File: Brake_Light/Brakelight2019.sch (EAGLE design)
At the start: 62 parts, among them J1 POWER_JACK, U1 R-78E5.0-1.0

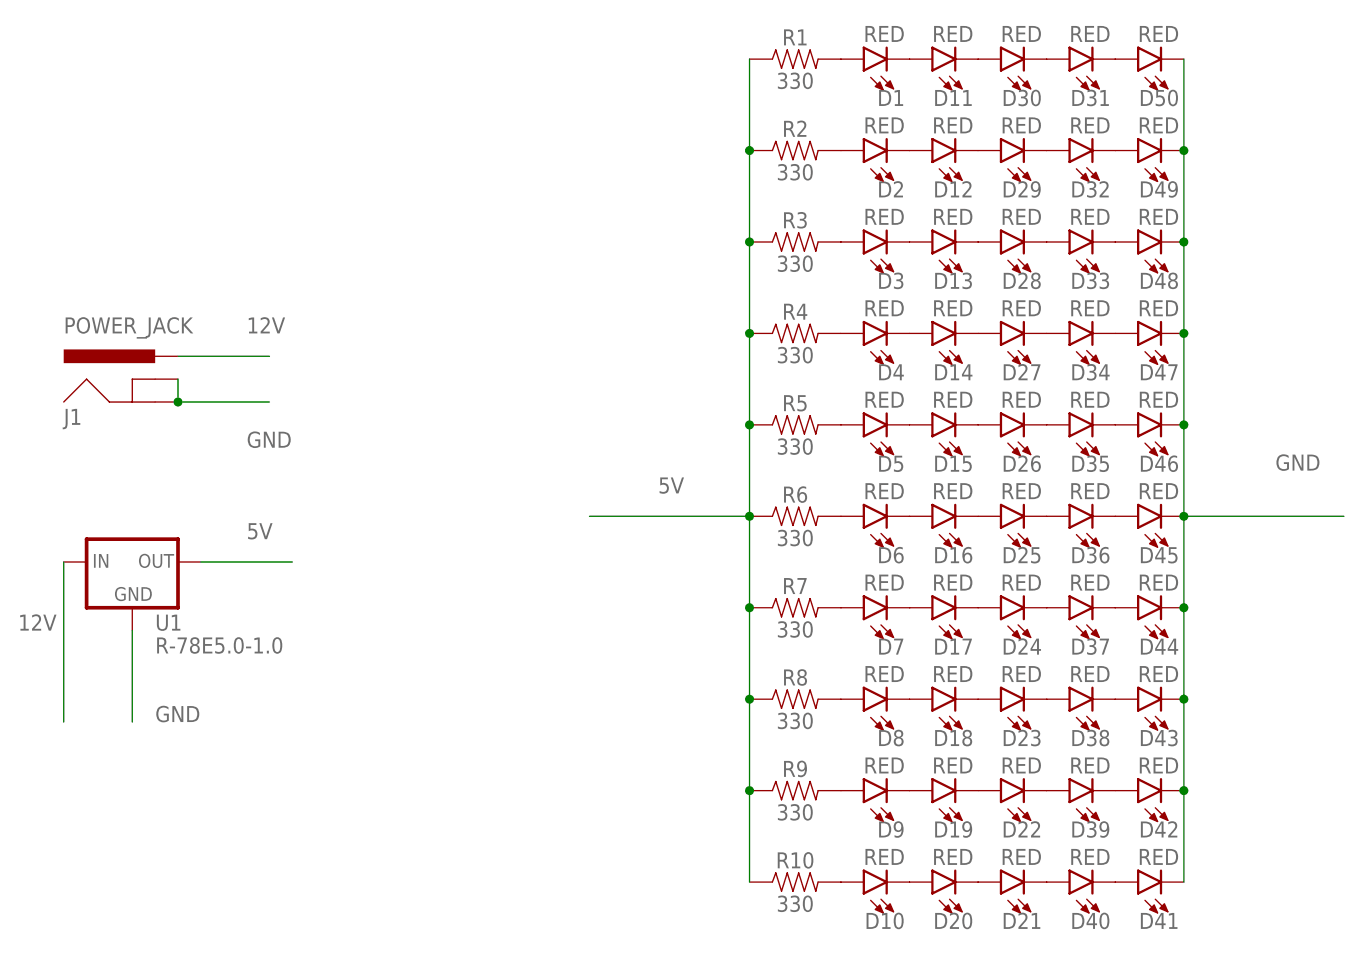
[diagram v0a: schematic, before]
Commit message: Add files via upload
changed out LEDs and voltage regulator for better ones.
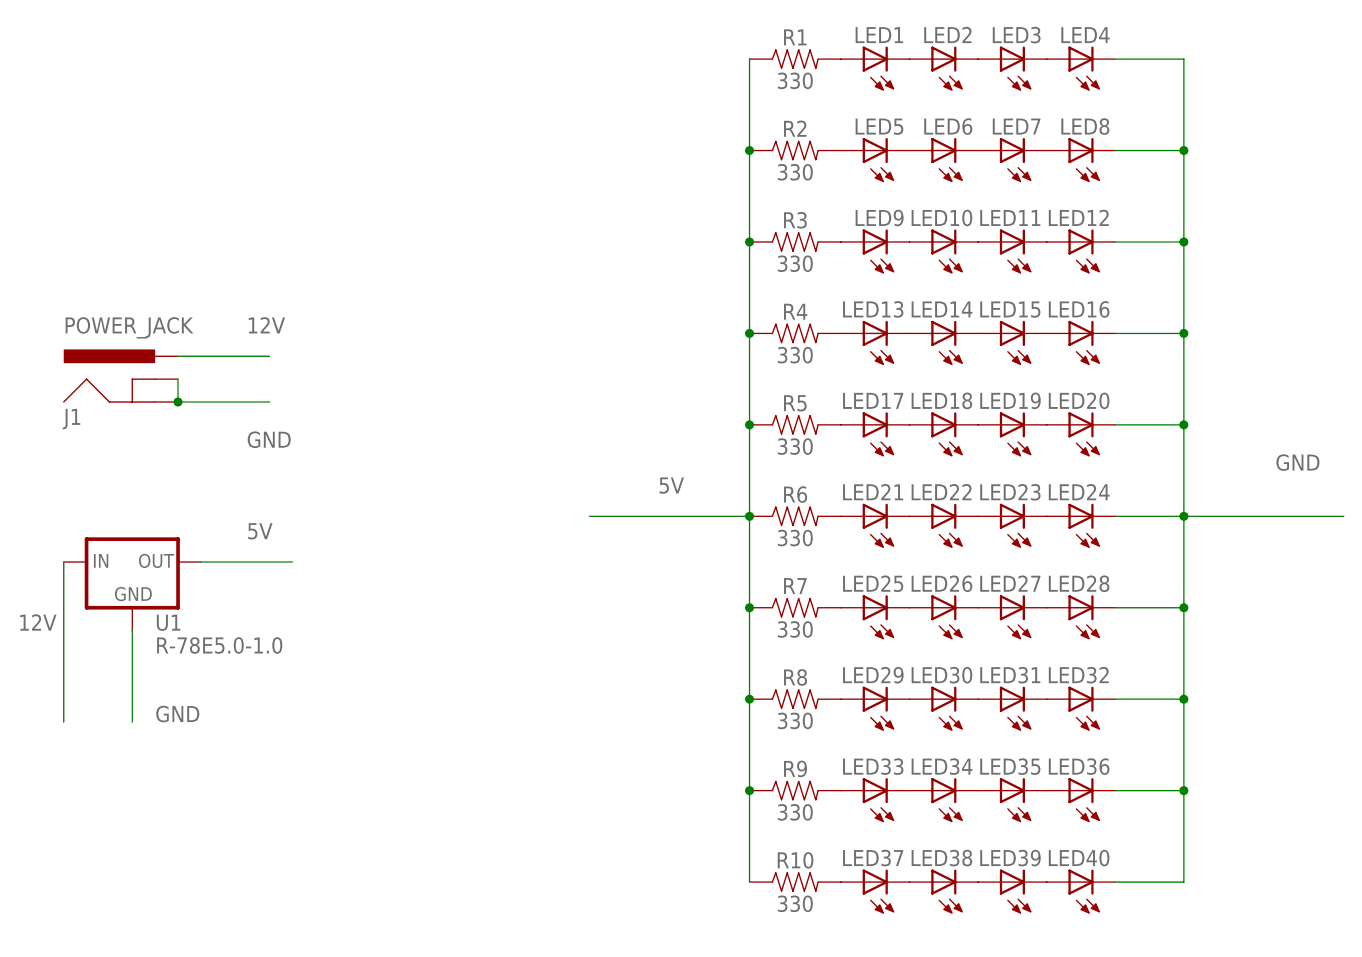
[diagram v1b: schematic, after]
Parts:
- removed D1, D10, D11, D12, D13, D14, D15, D16, D17, D18, D19, D2, D20, D21, D22, D23, D24, D25, D26, D27, D28, D29, D3, D30, D31, D32, D33, D34, D35, D36, D37, D38, D39, D4, D40, D41, D42, D43, D44, D45, D46, D47, D48, D49, D5, D50, D6, D7, D8, D9: RED, SparkFun-LED:LED-RED1206
- added LED1, LED10, LED11, LED12, LED13, LED14, LED15, LED16, LED17, LED18, LED19, LED2, LED20, LED21, LED22, LED23, LED24, LED25, LED26, LED27, LED28, LED29, LED3, LED30, LED31, LED32, LED33, LED34, LED35, LED36, LED37, LED38, LED39, LED4, LED40, LED5, LED6, LED7, LED8, LED9: (no value), adafruit:LED5MM
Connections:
- removed net N$41: D1.A, R1.2
- removed net N$42: D2.A, R2.2
- removed net N$43: D3.A, R3.2
- removed net N$44: D4.A, R4.2
- removed net N$45: D5.A, R5.2
- removed net N$46: D6.A, R6.2
- removed net N$47: D7.A, R7.2
- removed net N$48: D8.A, R8.2
- removed net N$49: D9.A, R9.2
- removed net N$50: D10.A, R10.2
- net GND: now also LED12.C, LED16.C, LED20.C, LED24.C, LED28.C, LED32.C, LED36.C, LED4.C, LED40.C, LED8.C; no longer D41.C, D42.C, D43.C, D44.C, D45.C, D46.C, D47.C, D48.C, D49.C, D50.C
- net N$1: now also LED1.A, R1.2; no longer D1.C, D11.A
- net N$10: now also LED10.A, LED9.C; no longer D10.C, D20.A
- net N$11: now also LED10.C, LED11.A; no longer D20.C, D21.A
- net N$12: now also LED11.C, LED12.A; no longer D19.C, D22.A
- net N$13: now also LED13.A, R4.2; no longer D18.C, D23.A
- net N$14: now also LED13.C, LED14.A; no longer D17.C, D24.A
- net N$15: now also LED14.C, LED15.A; no longer D16.C, D25.A
- net N$16: now also LED15.C, LED16.A; no longer D15.C, D26.A
- net N$17: now also LED17.A, R5.2; no longer D14.C, D27.A
- net N$18: now also LED17.C, LED18.A; no longer D13.C, D28.A
- net N$19: now also LED18.C, LED19.A; no longer D12.C, D29.A
- net N$2: now also LED1.C, LED2.A; no longer D12.A, D2.C
- net N$20: now also LED19.C, LED20.A; no longer D11.C, D30.A
- net N$21: now also LED21.A, R6.2; no longer D30.C, D31.A
- net N$22: now also LED21.C, LED22.A; no longer D29.C, D32.A
- net N$23: now also LED22.C, LED23.A; no longer D28.C, D33.A
- net N$24: now also LED23.C, LED24.A; no longer D27.C, D34.A
- net N$25: now also LED25.A, R7.2; no longer D26.C, D35.A
- net N$26: now also LED25.C, LED26.A; no longer D25.C, D36.A
- net N$27: now also LED26.C, LED27.A; no longer D24.C, D37.A
- net N$28: now also LED27.C, LED28.A; no longer D23.C, D38.A
- net N$29: now also LED29.A, R8.2; no longer D22.C, D39.A
- net N$3: now also LED2.C, LED3.A; no longer D13.A, D3.C
- net N$30: now also LED29.C, LED30.A; no longer D21.C, D40.A
- net N$31: now also LED30.C, LED31.A; no longer D40.C, D41.A
- net N$32: now also LED31.C, LED32.A; no longer D39.C, D42.A
- net N$33: now also LED33.A, R9.2; no longer D38.C, D43.A
- net N$34: now also LED33.C, LED34.A; no longer D37.C, D44.A
- net N$35: now also LED34.C, LED35.A; no longer D36.C, D45.A
- net N$36: now also LED35.C, LED36.A; no longer D35.C, D46.A
- net N$37: now also LED37.A, R10.2; no longer D34.C, D47.A
- net N$38: now also LED37.C, LED38.A; no longer D33.C, D48.A
- net N$39: now also LED38.C, LED39.A; no longer D32.C, D49.A
- net N$4: now also LED3.C, LED4.A; no longer D14.A, D4.C
- net N$40: now also LED39.C, LED40.A; no longer D31.C, D50.A
- net N$5: now also LED5.A, R2.2; no longer D15.A, D5.C
- net N$6: now also LED5.C, LED6.A; no longer D16.A, D6.C
- net N$7: now also LED6.C, LED7.A; no longer D17.A, D7.C
- net N$8: now also LED7.C, LED8.A; no longer D18.A, D8.C
- net N$9: now also LED9.A, R3.2; no longer D19.A, D9.C

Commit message: Add files via upload
Here you go tony
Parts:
- added 5V_BYPASS: (no value), SparkFun-Connectors:CONN_02
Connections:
- net 5V: now also 5V_BYPASS.1
- net GND: now also 5V_BYPASS.2
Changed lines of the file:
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@@
 <part name="LED39" library="adafruit" library_urn="urn:adsk.eagle:library:420" deviceset="LED" device="5MM" package3d_urn="urn:adsk.eagle:package:6240538/1"/>
 <part name="LED40" library="adafruit" library_urn="urn:adsk.eagle:library:420" deviceset="LED" device="5MM" package3d_urn="urn:adsk.eagle:package:6240538/1"/>
+<part name="5V_BYPASS" library="SparkFun-Connectors" library_urn="urn:adsk.eagle:library:513" deviceset="CONN_02" device="" package3d_urn="urn:adsk.eagle:package:38039/1"/>
 </parts>
 <sheets>
@@
 <instance part="LED39" gate="G$1" x="116.84" y="40.64" rot="R90"/>
 <instance part="LED40" gate="G$1" x="124.46" y="40.64" rot="R90"/>
+<instance part="5V_BYPASS" gate="G$1" x="27.94" y="119.38"/>
 </instances>
 <busses>
@@
 <wire x1="129.54" y1="40.64" x2="137.16" y2="40.64" width="0.1524" layer="91"/>
 </segment>
+<segment>
+<pinref part="5V_BYPASS" gate="G$1" pin="2"/>
+<wire x1="35.56" y1="121.92" x2="35.56" y2="124.46" width="0.1524" layer="91"/>
+<wire x1="35.56" y1="124.46" x2="45.72" y2="124.46" width="0.1524" layer="91"/>
+<label x="43.18" y="127" size="1.778" layer="95"/>
+</segment>
 </net>
 <net name="5V" class="0">
@@
 <label x="78.74" y="83.82" size="1.778" layer="95"/>
 </segment>
+<segment>
+<pinref part="5V_BYPASS" gate="G$1" pin="1"/>
+<wire x1="35.56" y1="119.38" x2="45.72" y2="119.38" width="0.1524" layer="91"/>
+<label x="43.18" y="114.3" size="1.778" layer="95"/>
+</segment>
 </net>

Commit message: Add files via upload
Changed LED configuration and removed 5V capability
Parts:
- removed 5V_BYPASS: (no value), SparkFun-Connectors:CONN_02
- removed LED33, LED34, LED35, LED36, LED37, LED38, LED39, LED40: (no value), adafruit:LED5MM
- removed R10, R9: 330, SparkFun-Resistors:330OHM-0603-1/10W-1%
- removed U1: R-78E5.0-1.0, SparkFun-IC-Power:R-78E5.0-1.0
- added LED41, LED42, LED43, LED44, LED45, LED46, LED47, LED48: (no value), adafruit:LED5MM
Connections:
- removed net N$33: LED33.A, R9.2
- removed net N$34: LED33.C, LED34.A
- removed net N$35: LED34.C, LED35.A
- removed net N$36: LED35.C, LED36.A
- removed net N$37: LED37.A, R10.2
- removed net N$38: LED37.C, LED38.A
- removed net N$39: LED38.C, LED39.A
- removed net N$40: LED39.C, LED40.A
- new net N$41: LED4.C, LED41.A
- new net N$42: LED42.A, LED8.C
- new net N$43: LED12.C, LED43.A
- new net N$44: LED16.C, LED44.A
- new net N$45: LED20.C, LED45.A
- new net N$46: LED24.C, LED46.A
- new net N$47: LED28.C, LED47.A
- new net N$48: LED32.C, LED48.A
- net 12V: no longer U1.IN
- net 5V: no longer 5V_BYPASS.1, R10.1, R9.1, U1.OUT
- net GND: now also LED41.C, LED42.C, LED43.C, LED44.C, LED45.C, LED46.C, LED47.C, LED48.C; no longer 5V_BYPASS.2, LED12.C, LED16.C, LED20.C, LED24.C, LED28.C, LED32.C, LED36.C, LED4.C, LED40.C, LED8.C, U1.GND

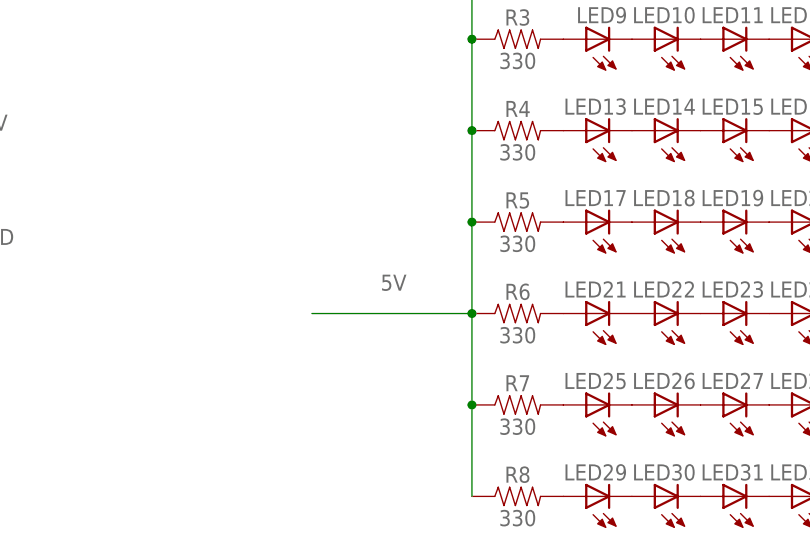
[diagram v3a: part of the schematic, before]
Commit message: Add files via upload
Unfucked the Ground and Power planes
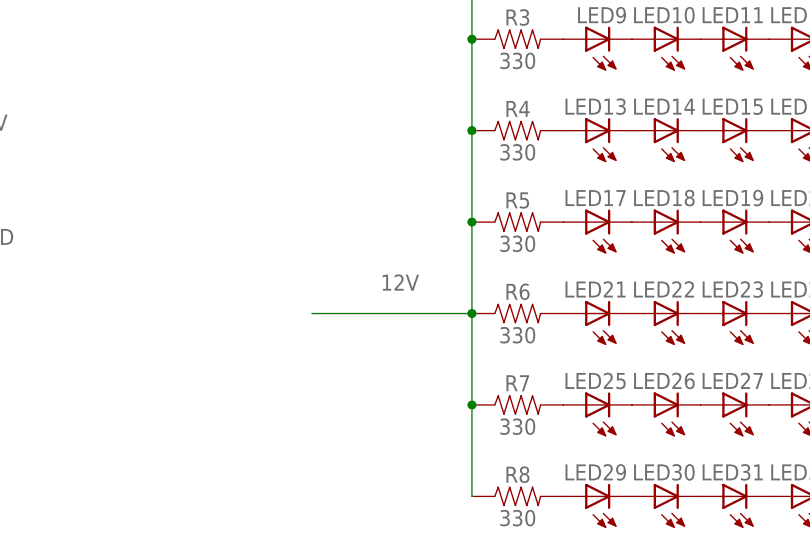
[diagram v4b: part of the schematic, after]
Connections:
- removed net 5V: R1.1, R2.1, R3.1, R4.1, R5.1, R6.1, R7.1, R8.1
- net 12V: now also R1.1, R2.1, R3.1, R4.1, R5.1, R6.1, R7.1, R8.1
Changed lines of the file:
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@@
 <label x="33.02" y="101.6" size="1.778" layer="95"/>
+</segment>
+<segment>
+<pinref part="R1" gate="G$1" pin="1"/>
+<pinref part="R2" gate="G$1" pin="1"/>
+<wire x1="88.9" y1="132.08" x2="88.9" y2="121.92" width="0.1524" layer="91"/>
+<pinref part="R3" gate="G$1" pin="1"/>
+<wire x1="88.9" y1="121.92" x2="88.9" y2="111.76" width="0.1524" layer="91"/>
+<junction x="88.9" y="121.92"/>
+<pinref part="R4" gate="G$1" pin="1"/>
+<wire x1="88.9" y1="111.76" x2="88.9" y2="101.6" width="0.1524" layer="91"/>
+<junction x="88.9" y="111.76"/>
+<pinref part="R5" gate="G$1" pin="1"/>
+<wire x1="88.9" y1="101.6" x2="88.9" y2="91.44" width="0.1524" layer="91"/>
+<junction x="88.9" y="101.6"/>
+<pinref part="R6" gate="G$1" pin="1"/>
+<wire x1="88.9" y1="91.44" x2="88.9" y2="81.28" width="0.1524" layer="91"/>
+<junction x="88.9" y="91.44"/>
+<pinref part="R7" gate="G$1" pin="1"/>
+<wire x1="88.9" y1="81.28" x2="88.9" y2="71.12" width="0.1524" layer="91"/>
+<junction x="88.9" y="81.28"/>
+<pinref part="R8" gate="G$1" pin="1"/>
+<wire x1="88.9" y1="71.12" x2="88.9" y2="60.96" width="0.1524" layer="91"/>
+<junction x="88.9" y="71.12"/>
+<wire x1="88.9" y1="81.28" x2="71.12" y2="81.28" width="0.1524" layer="91"/>
+<label x="78.74" y="83.82" size="1.778" layer="95"/>
 </segment>
 </net>
@@
 </segment>
 </net>
-<net name="5V" class="0">
-<segment>
-<pinref part="R1" gate="G$1" pin="1"/>
-<pinref part="R2" gate="G$1" pin="1"/>
-<wire x1="88.9" y1="132.08" x2="88.9" y2="121.92" width="0.1524" layer="91"/>
-<pinref part="R3" gate="G$1" pin="1"/>
-<wire x1="88.9" y1="121.92" x2="88.9" y2="111.76" width="0.1524" layer="91"/>
-<junction x="88.9" y="121.92"/>
-<pinref part="R4" gate="G$1" pin="1"/>
-<wire x1="88.9" y1="111.76" x2="88.9" y2="101.6" width="0.1524" layer="91"/>
-<junction x="88.9" y="111.76"/>
-<pinref part="R5" gate="G$1" pin="1"/>
-<wire x1="88.9" y1="101.6" x2="88.9" y2="91.44" width="0.1524" layer="91"/>
-<junction x="88.9" y="101.6"/>
-<pinref part="R6" gate="G$1" pin="1"/>
-<wire x1="88.9" y1="91.44" x2="88.9" y2="81.28" width="0.1524" layer="91"/>
-<junction x="88.9" y="91.44"/>
-<pinref part="R7" gate="G$1" pin="1"/>
-<wire x1="88.9" y1="81.28" x2="88.9" y2="71.12" width="0.1524" layer="91"/>
-<junction x="88.9" y="81.28"/>
-<pinref part="R8" gate="G$1" pin="1"/>
-<wire x1="88.9" y1="71.12" x2="88.9" y2="60.96" width="0.1524" layer="91"/>
-<junction x="88.9" y="71.12"/>
-<wire x1="88.9" y1="81.28" x2="71.12" y2="81.28" width="0.1524" layer="91"/>
-<label x="78.74" y="83.82" size="1.778" layer="95"/>
-</segment>
-</net>

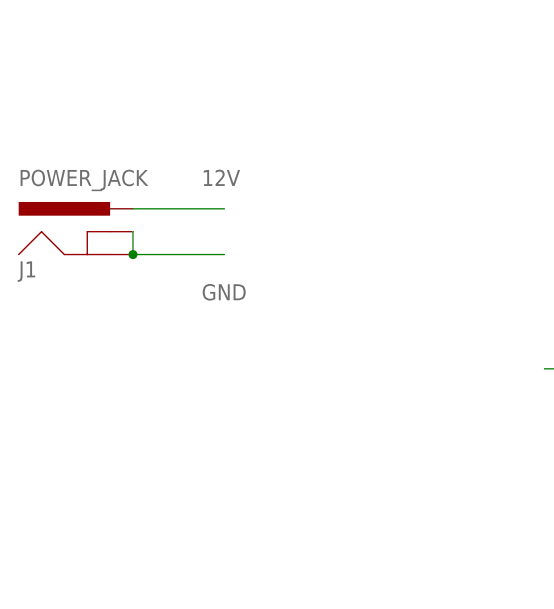
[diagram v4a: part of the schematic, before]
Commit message: Add files via upload
Changed to Molex connector
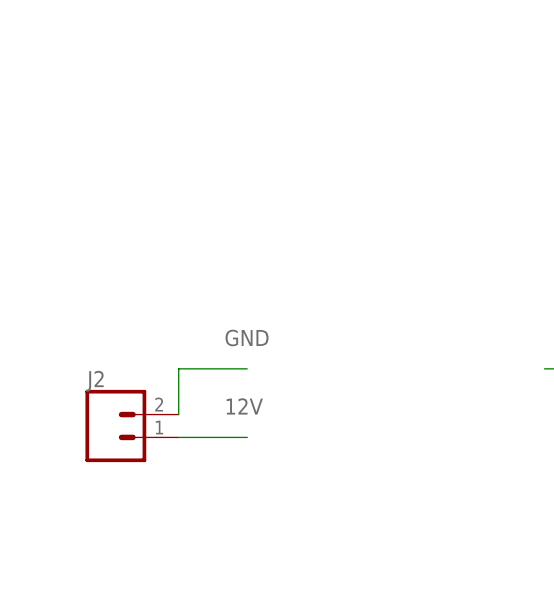
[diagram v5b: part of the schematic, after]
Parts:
- removed J1: POWER_JACK, SparkFun-Connectors:POWER_JACK
- added J2: (no value), SparkFun-Connectors:CONN_02POLAR
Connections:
- net 12V: now also J2.1; no longer J1.PWR
- net GND: now also J2.2; no longer J1.GND, J1.GNDBREAK
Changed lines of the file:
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@@
 </classes>
 <parts>
-<part name="J1" library="SparkFun-Connectors" library_urn="urn:adsk.eagle:library:513" deviceset="POWER_JACK" device="" package3d_urn="urn:adsk.eagle:package:38231/1"/>
 <part name="R1" library="SparkFun-Resistors" library_urn="urn:adsk.eagle:library:532" deviceset="330OHM" device="-0603-1/10W-1%" package3d_urn="urn:adsk.eagle:package:39650/1" value="330"/>
 <part name="R2" library="SparkFun-Resistors" library_urn="urn:adsk.eagle:library:532" deviceset="330OHM" device="-0603-1/10W-1%" package3d_urn="urn:adsk.eagle:package:39650/1" value="330"/>
@@
 <part name="LED47" library="adafruit" library_urn="urn:adsk.eagle:library:420" deviceset="LED" device="5MM" package3d_urn="urn:adsk.eagle:package:6240538/1"/>
 <part name="LED48" library="adafruit" library_urn="urn:adsk.eagle:library:420" deviceset="LED" device="5MM" package3d_urn="urn:adsk.eagle:package:6240538/1"/>
+<part name="J2" library="SparkFun-Connectors" library_urn="urn:adsk.eagle:library:513" deviceset="CONN_02" device="POLAR" package3d_urn="urn:adsk.eagle:package:38040/1"/>
 </parts>
 <sheets>
@@
 </plain>
 <instances>
-<instance part="J1" gate="G$1" x="22.86" y="91.44"/>
 <instance part="R1" gate="G$1" x="93.98" y="132.08"/>
 <instance part="R2" gate="G$1" x="93.98" y="121.92"/>
@@
 <instance part="LED47" gate="G$1" x="132.08" y="71.12" rot="R90"/>
 <instance part="LED48" gate="G$1" x="132.08" y="60.96" rot="R90"/>
+<instance part="J2" gate="G$1" x="22.86" y="73.66"/>
 </instances>
 <busses>
@@
 <nets>
 <net name="12V" class="0">
-<segment>
-<pinref part="J1" gate="G$1" pin="PWR"/>
-<wire x1="25.4" y1="99.06" x2="35.56" y2="99.06" width="0.1524" layer="91"/>
-<label x="33.02" y="101.6" size="1.778" layer="95"/>
-</segment>
 <segment>
 <pinref part="R1" gate="G$1" pin="1"/>
@@
 <label x="78.74" y="83.82" size="1.778" layer="95"/>
 </segment>
+<segment>
+<pinref part="J2" gate="G$1" pin="1"/>
+<wire x1="30.48" y1="73.66" x2="38.1" y2="73.66" width="0.1524" layer="91"/>
+<label x="35.56" y="76.2" size="1.778" layer="95"/>
+</segment>
 </net>
 <net name="GND" class="0">
-<segment>
-<pinref part="J1" gate="G$1" pin="GNDBREAK"/>
-<pinref part="J1" gate="G$1" pin="GND"/>
-<wire x1="25.4" y1="96.52" x2="25.4" y2="93.98" width="0.1524" layer="91"/>
-<wire x1="25.4" y1="93.98" x2="35.56" y2="93.98" width="0.1524" layer="91"/>
-<junction x="25.4" y="93.98"/>
-<label x="33.02" y="88.9" size="1.778" layer="95"/>
-</segment>
 <segment>
 <wire x1="137.16" y1="132.08" x2="137.16" y2="121.92" width="0.1524" layer="91"/>
@@
 <pinref part="LED48" gate="G$1" pin="C"/>
 </segment>
+<segment>
+<pinref part="J2" gate="G$1" pin="2"/>
+<wire x1="30.48" y1="76.2" x2="30.48" y2="81.28" width="0.1524" layer="91"/>
+<wire x1="30.48" y1="81.28" x2="38.1" y2="81.28" width="0.1524" layer="91"/>
+<label x="35.56" y="83.82" size="1.778" layer="95"/>
+</segment>
 </net>
